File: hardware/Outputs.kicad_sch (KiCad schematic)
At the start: 0 parts

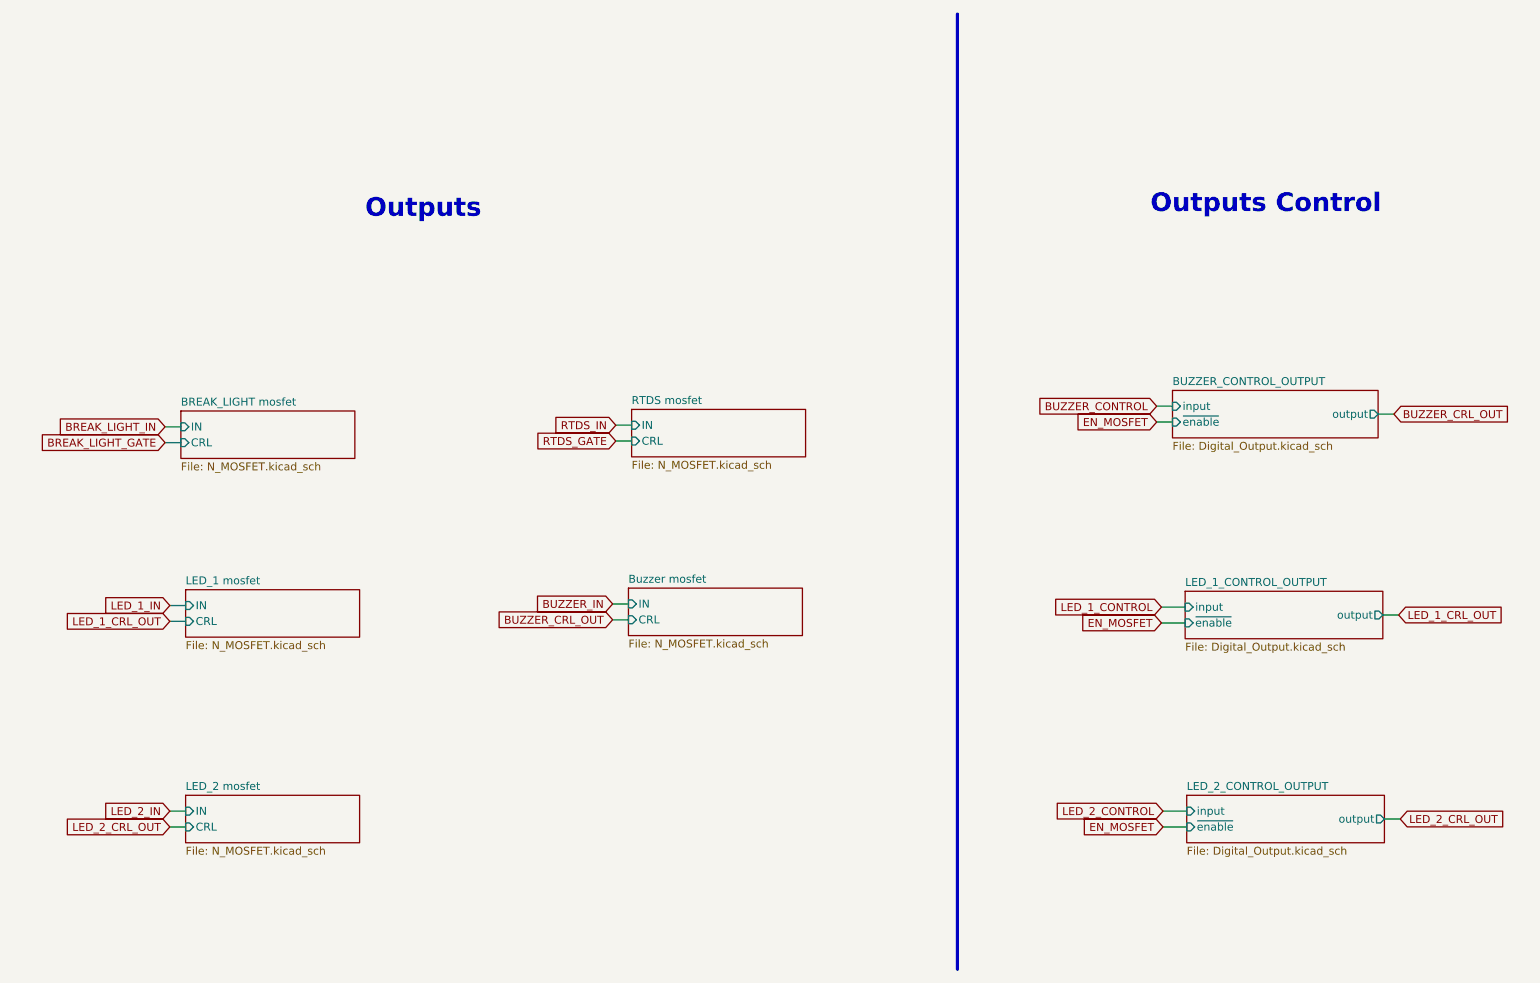
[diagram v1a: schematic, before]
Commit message: major schematic update, changed optocouplers for different, added new fuses for 5v supply for water and potentiometers and 24v supply for BSPD/ESB, updated autosport connector, and some other changes
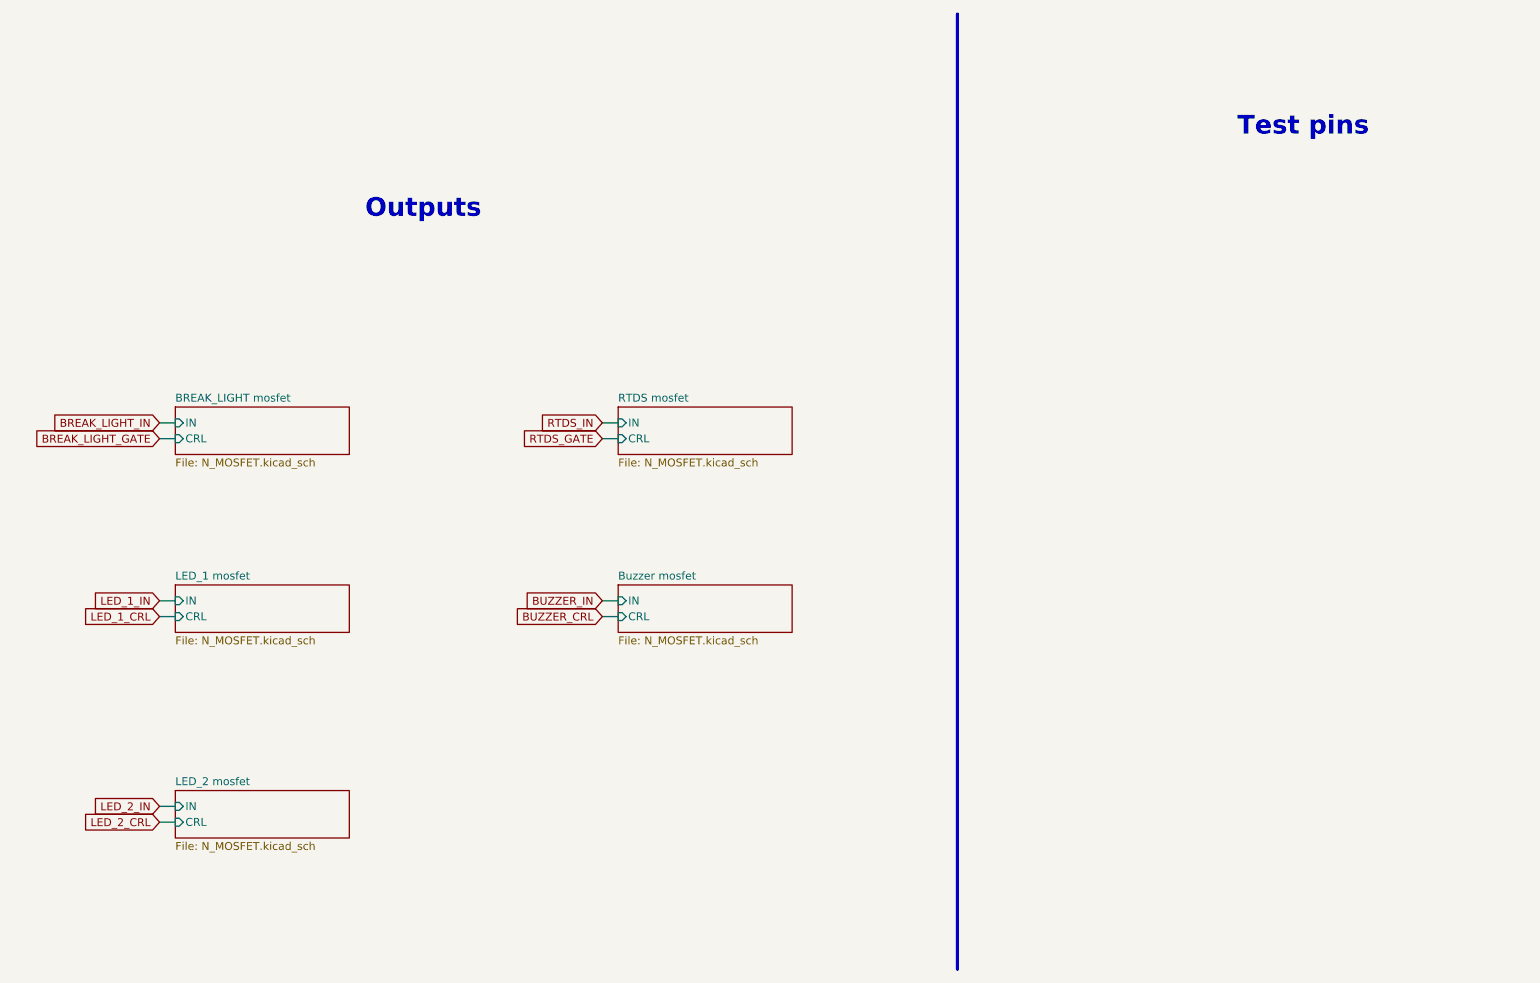
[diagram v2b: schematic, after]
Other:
- removed sheet BUZZER_CONTROL_OUTPUT
- removed sheet LED_1_CONTROL_OUTPUT
- removed sheet LED_2_CONTROL_OUTPUT
- note added: "Test pins"
- note removed: "Outputs Control"

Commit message: changed some footprints for clarity, and made some progress on board
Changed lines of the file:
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@@
+    )
+  )
+  (global_label "BUZZER_CONTROL" (shape input) (at 120.015 109.22 180) (fields_autoplaced)
+    (effects (font (size 1.27 1.27)) (justify right))
+    (property "Intersheet References" "${INTERSHEET_REFS}" (id 0) (at 395.605 262.89 0)
+      (effects (font (size 1.27 1.27)) hide)
+    )
+  )
+  (global_label "LED_1_CONTROL" (shape input) (at 48.895 109.22 180) (fields_autoplaced)
+    (effects (font (size 1.27 1.27)) (justify right))
+    (property "Intersheet References" "${INTERSHEET_REFS}" (id 0) (at 324.485 257.81 0)
+      (effects (font (size 1.27 1.27)) hide)
     )
   )
@@
     )
   )
-  (global_label "LED_2_CRL" (shape input) (at 48.895 142.24 180) (fields_autoplaced)
-    (effects (font (size 1.27 1.27)) (justify right))
-    (property "Intersheet References" "${INTERSHEET_REFS}" (id 0) (at 36.4108 142.1606 0)
-      (effects (font (size 1.27 1.27)) (justify right) hide)
-    )
-  )
   (global_label "RTDS_GATE" (shape input) (at 120.015 80.645 180) (fields_autoplaced)
     (effects (font (size 1.27 1.27)) (justify right))
     (property "Intersheet References" "${INTERSHEET_REFS}" (id 0) (at -95.885 37.465 0)
+      (effects (font (size 1.27 1.27)) hide)
+    )
+  )
+  (global_label "LED_2_CONTROL" (shape input) (at 48.895 142.24 180) (fields_autoplaced)
+    (effects (font (size 1.27 1.27)) (justify right))
+    (property "Intersheet References" "${INTERSHEET_REFS}" (id 0) (at 324.485 288.29 0)
       (effects (font (size 1.27 1.27)) hide)
     )
@@
     )
   )
-  (global_label "BUZZER_CRL" (shape input) (at 120.015 109.22 180) (fields_autoplaced)
-    (effects (font (size 1.27 1.27)) (justify right))
-    (property "Intersheet References" "${INTERSHEET_REFS}" (id 0) (at 105.7165 109.1406 0)
-      (effects (font (size 1.27 1.27)) (justify right) hide)
-    )
-  )
-  (global_label "LED_1_CRL" (shape input) (at 48.895 109.22 180) (fields_autoplaced)
-    (effects (font (size 1.27 1.27)) (justify right))
-    (property "Intersheet References" "${INTERSHEET_REFS}" (id 0) (at 36.4108 109.1406 0)
-      (effects (font (size 1.27 1.27)) (justify right) hide)
-    )
-  )
